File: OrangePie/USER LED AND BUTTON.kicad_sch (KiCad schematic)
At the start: 0 parts

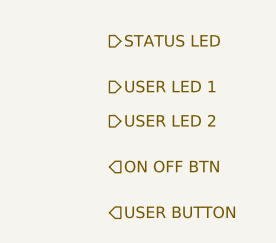
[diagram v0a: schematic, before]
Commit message: Add CH340 debug
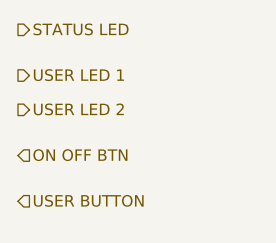
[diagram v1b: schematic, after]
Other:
- company: (none) -> ModuCard System
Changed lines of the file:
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@@
 	(generator_version "8.0")
 	(paper "A4")
+	(title_block
+		(date "2025-02-10")
+		(rev "A")
+		(company "ModuCard System")
+	)
 	(hierarchical_label "USER BUTTON"
 		(shape input)
-		(at 91.44 125.73 0)
+		(at 81.28 124.46 0)
 		(fields_autoplaced yes)
 		(effects
@@
 	(hierarchical_label "USER LED 1"
 		(shape output)
-		(at 91.44 111.76 0)
+		(at 81.28 110.49 0)
 		(fields_autoplaced yes)
 		(effects
@@
 	(hierarchical_label "USER LED 2"
 		(shape output)
-		(at 91.44 115.57 0)
+		(at 81.28 114.3 0)
 		(fields_autoplaced yes)
 		(effects
@@
 	(hierarchical_label "ON OFF BTN"
 		(shape input)
-		(at 91.44 120.65 0)
+		(at 81.28 119.38 0)
 		(fields_autoplaced yes)
 		(effects
@@
 	(hierarchical_label "STATUS LED"
 		(shape output)
-		(at 91.44 106.68 0)
+		(at 81.28 105.41 0)
 		(fields_autoplaced yes)
 		(effects
